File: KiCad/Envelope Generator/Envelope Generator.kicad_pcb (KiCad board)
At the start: 2 copper layers, 78 x 57 mm, 65 parts, among them J1 Screw_Terminal_01x03, J2 Screw_Terminal_01x03, U1 TL074, U2 TL074, U3 TL074

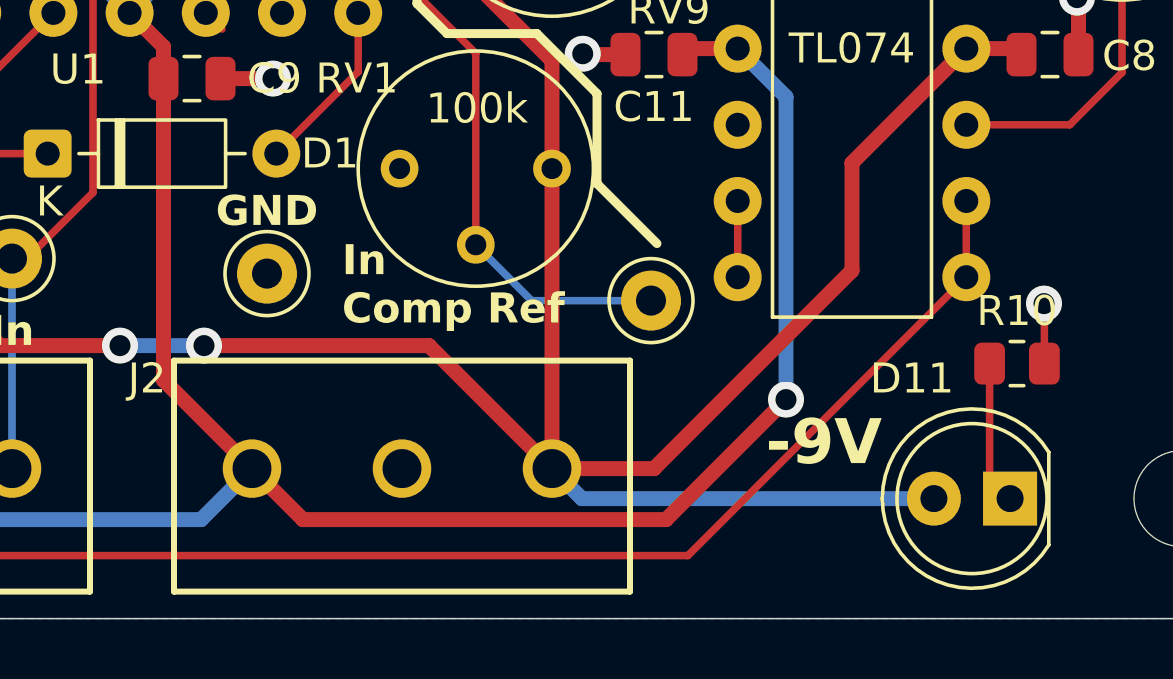
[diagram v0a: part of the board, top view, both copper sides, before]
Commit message: preparation to merge project back into one board
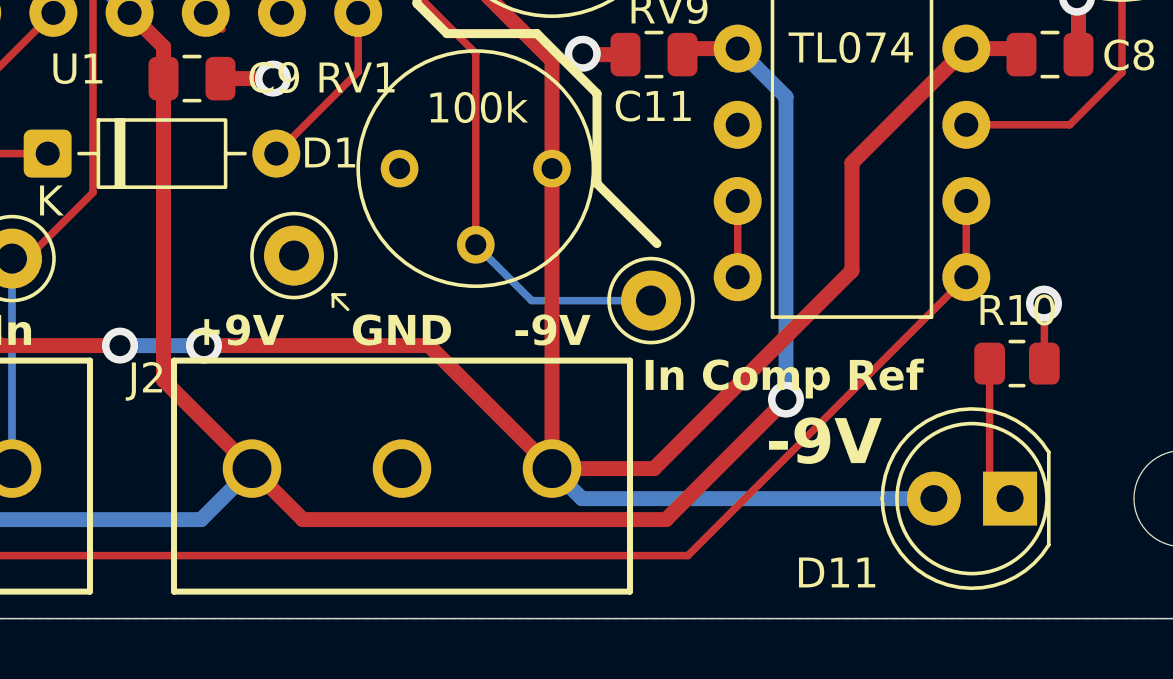
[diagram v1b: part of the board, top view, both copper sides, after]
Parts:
- moved TP7 1.08 mm to (58.4, 106.9)
- renumbered TP5 to TP1, TP6 to TP2, TP4 to TP3, TP7 to TP4, TP8 to TP5, TP9 to TP6, TP12 to TP7, TP1 to TP8
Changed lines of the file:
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@@
 			(plot_on_all_layers_selection 0x00000000_00000000_00000000_00000000)
 			(disableapertmacros no)
-			(usegerberextensions no)
+			(usegerberextensions yes)
 			(usegerberattributes yes)
 			(usegerberadvancedattributes yes)
-			(creategerberjobfile yes)
+			(creategerberjobfile no)
 			(dashed_line_dash_ratio 12)
 			(dashed_line_gap_ratio 3)
@@
 			(outputformat 1)
 			(mirror no)
-			(drillshape 1)
+			(drillshape 0)
 			(scaleselection 1)
-			(outputdirectory "")
+			(outputdirectory "../../Build/Aug 20 2026/")
 		)
 	)
@@
 		(descr "Keystone THM Miniature Test Point 5000-5004, http://www.keyelco.com/product-pdf.cfm?p=1309")
 		(tags "Through Hole Mount Test Points")
-		(property "Reference" "TP4"
+		(property "Reference" "TP3"
 			(at 0 -2.5 0)
 			(layer "F.SilkS")
@@
 		(descr "Keystone THM Miniature Test Point 5000-5004, http://www.keyelco.com/product-pdf.cfm?p=1309")
 		(tags "Through Hole Mount Test Points")
-		(property "Reference" "TP6"
+		(property "Reference" "TP2"
 			(at 0 -2.5 0)
 			(layer "F.SilkS")
@@
 		(descr "Keystone THM Miniature Test Point 5000-5004, http://www.keyelco.com/product-pdf.cfm?p=1309")
 		(tags "Through Hole Mount Test Points")
-		(property "Reference" "TP8"
+		(property "Reference" "TP5"
 			(at 0 -2.5 0)
 			(layer "F.SilkS")
@@
 		(tags "LED")
 		(property "Reference" "D11"
-			(at 3.27 4 0)
+			(at 5.77 -2.5 0)
 			(layer "F.SilkS")
 			(effects
@@
 		(descr "Keystone THM Miniature Test Point 5000-5004, http://www.keyelco.com/product-pdf.cfm?p=1309")
 		(tags "Through Hole Mount Test Points")
-		(property "Reference" "TP7"
+		(property "Reference" "TP4"
 			(at 0 -2.5 0)
 			(layer "F.SilkS")
@@
 		(descr "Keystone THM Miniature Test Point 5000-5004, http://www.keyelco.com/product-pdf.cfm?p=1309")
 		(tags "Through Hole Mount Test Points")
-		(property "Reference" "TP1"
+		(property "Reference" "TP8"
 			(at 0 -2.5 0)
 			(layer "F.SilkS")
@@
 		(descr "Keystone THM Miniature Test Point 5000-5004, http://www.keyelco.com/product-pdf.cfm?p=1309")
 		(tags "Through Hole Mount Test Points")
-		(property "Reference" "TP9"
+		(property "Reference" "TP6"
 			(at 0 -2.5 0)
 			(layer "F.SilkS")
@@
 	(footprint "TestPoint:TestPoint_Keystone_5000-5004_Miniature"
 		(layer "F.Cu")
-		(at 57.5 107.5)
+		(at 58.4 106.9)
 		(descr "Keystone THM Miniature Test Point 5000-5004, http://www.keyelco.com/product-pdf.cfm?p=1309")
 		(tags "Through Hole Mount Test Points")
-		(property "Reference" "TP12"
+		(property "Reference" "TP7"
 			(at 0 -2.5 0)
 			(layer "F.SilkS")
@@
 		(descr "Keystone THM Miniature Test Point 5000-5004, http://www.keyelco.com/product-pdf.cfm?p=1309")
 		(tags "Through Hole Mount Test Points")
-		(property "Reference" "TP5"
+		(property "Reference" "TP1"
 			(at 0 -2.5 0)
 			(layer "F.SilkS")
@@
 	)
 	(gr_line
+		(start 59.7 108.2)
+		(end 59.7 108.6)
+		(stroke
+			(width 0.1)
+			(type default)
+		)
+		(layer "F.SilkS")
+	)
+	(gr_line
+		(start 59.7 108.2)
+		(end 60.1 108.2)
+		(stroke
+			(width 0.1)
+			(type default)
+		)
+		(layer "F.SilkS")
+	)
+	(gr_line
+		(start 59.7 108.2)
+		(end 60.2 108.7)
+		(stroke
+			(width 0.1)
+			(type default)
+		)
+		(layer "F.SilkS")
+	)
+	(gr_line
 		(start 61 89.5)
 		(end 56.5 89.5)
@@
 		)
 	)
-	(gr_text "In\nComp Ref"
-		(at 60 109.25 0)
+	(gr_text "In Comp Ref"
+		(at 70 111.5 0)
 		(layer "F.SilkS")
 		(effects
@@
 		)
 	)
+	(gr_text "+9V"
+		(at 56.5 110 0)
+		(layer "F.SilkS")
+		(effects
+			(font
+				(size 1 1)
+				(thickness 0.2)
+				(bold yes)
+			)
+			(justify bottom)
+		)
+	)
 	(gr_text "GND"
-		(at 57.5 106 0)
+		(at 62 110 0)
 		(layer "F.SilkS")
 		(effects
@@
 		(layer "F.SilkS")
 		(effects
+			(font
+				(size 1 1)
+				(thickness 0.2)
+				(bold yes)
+			)
+			(justify bottom)
+		)
+	)
+	(gr_text "-9V"
+		(at 67 110 0)
+		(layer "F.SilkS")
+		(effects

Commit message: merged project into one combined board (excluding the buttons)
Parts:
- renumbered C1 to C16, C2 to C17, C3 to C18, C4 to C19, C5 to C20, C6 to C21, C7 to C22, C8 to C23, C9 to C24, C10 to C25, C11 to C26, D1 to D13, D2 to D14, D3 to D15, D4 to D16, D5 to D17, D6 to D18, D7 to D19, D8 to D20, D9 to D21, D10 to D22, D11 to D23, H1 to H13, H2 to H14, H3 to H15, H4 to H16, J1 to J7, J2 to J8, R1 to R33, R2 to R34, R3 to R35, R4 to R36, R5 to R37, R6 to R38, R7 to R39, R8 to R40, R9 to R41, R10 to R42, RV1 to RV10, RV2 to RV11, RV3 to RV12, RV4 to RV13, RV5 to RV14, RV6 to RV15, RV7 to RV16, RV8 to RV17, RV9 to RV18, RV10 to RV19, RV11 to RV20, RV12 to RV21, RV13 to RV22, RV14 to RV23, RV15 to RV24, TP8 to TP17, TP3 to TP18, TP1 to TP19, TP2 to TP20, TP4 to TP21, TP5 to TP22, TP6 to TP23, TP7 to TP24, U1 to U5, U2 to U6, U3 to U7
